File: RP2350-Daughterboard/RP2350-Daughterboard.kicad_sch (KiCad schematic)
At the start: 0 parts

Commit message: Added HDMI and PSRAM
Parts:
- added C1, C2: 15pF, symbol Device:C
- added C10, C3, C4, C7: 100nF, symbol Device:C
- added C5, C6: 4.7uF, symbol Device:C
- added C8: 1uF, Capacitor_SMD:C_0603_1608Metric, symbol Device:C
- added C9: 1uF, symbol Device:C
- added J1: ISA16_DAUGHTER_BUS, symbol W65C816-Computer:ISA16_DAUGHTER_BUS_98
- added J2: SWD, symbol Connector_Generic:Conn_01x05
- added J5: HDMI_A, symbol Connector:HDMI_A
- added L1: 2.2uH, symbol Device:L
- added R1: 1k, symbol Device:R
- added R10, R11, R12, R13, R6, R7, R8, R9: 270R, symbol Device:R
- added R14, R2, R3, R4, R5: 10k, symbol Device:R
- added SW1: BOOTSEL, symbol Switch:SW_Push
- added SW2: RESET, symbol Switch:SW_Push
- added U1: RP2354B, Package_DFN_QFN:QFN-80-1EP_10x10mm_P0.4mm_EP3.4x3.4mm, symbol MCU_RaspberryPi:RP2354B
- added U2: APS6404L-3SQR-SN, Package_SO:SOIC-8_3.9x4.9mm_P1.27mm, symbol Memory_RAM:APS6404L-3SQRx-SN
- added U3: TPD8F003, symbol Power_Protection:TPD8F003
- added Y1: 12MHz ABM8-272-T3, symbol Device:Crystal
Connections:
- new net +1V1: C4.1, C6.1, L1.2, U1.10 (DVDD), U1.32 (DVDD), U1.51 (DVDD), U1.65 (VREG_FB)
- new net +3V3: C10.1, C3.1, C5.1, C8.1, J1.2, J1.20, J1.42, J1.78, J2.1 (Pin_1), R14.1, R2.1, R3.1, R4.1, R5.1, U1.15 (IOVDD), U1.24 (IOVDD), U1.29 (IOVDD), U1.41 (IOVDD), U1.5 (IOVDD), U1.50 (IOVDD), U1.59 (ADC_AVDD), U1.60 (IOVDD), U1.61 (VREG_AVDD), U1.64 (VREG_VIN), U1.68 (USB_OTP_VDD), U1.69 (QSPI_IOVDD), U1.76 (IOVDD), U2.8 (VDD)
- new net +5V: C9.1, J1.38, J1.40, J5.18 (+5V)
- new net A0: J1.3, U1.77 (GPIO0)
- new net A1: J1.5, U1.78 (GPIO1)
- new net A10: J1.25
- new net A11: J1.27
- new net A12: J1.29
- new net A13: J1.31
- new net A14: J1.33
- new net A15: J1.35
- new net A16: J1.22
- new net A17: J1.24
- new net A18: J1.26
- new net A19: J1.28
- new net A2: J1.7, U1.79 (GPIO2)
- new net A20: J1.30
- new net A21: J1.32
- new net A22: J1.34
- new net A23: J1.36
- new net A3: J1.9, U1.80 (GPIO3)
- new net A4: J1.11, U1.1 (GPIO4)
- new net A5: J1.13, U1.2 (GPIO5)
- new net A6: J1.15, U1.3 (GPIO6)
- new net A7: J1.17, U1.4 (GPIO7)
- new net A8: J1.21, U1.6 (GPIO8)
- new net A9: J1.23, U1.7 (GPIO9)
- new net ABORT_N: J1.52
- new net AUDIO_IRQ: J1.71
- new net BANK00: J1.57
- new net BANK00_N: J1.58
- new net BE: J1.51
- new net DB_GPIO0: J1.74
- new net DB_GPIO1: J1.75
- new net DB_GPIO2: J1.76
- new net DB_GPIO3: J1.79
- new net DMA_ACK: J1.68
- new net DMA_REQ: J1.67
- new net E: J1.55
- new net EXP_CS_N: J1.73
- new net FRAME_IRQ: J1.70
- new net GND: C1.2, C10.2, C2.2, C3.2, C4.2, C5.2, C6.2, C7.2, C8.2, C9.2, J1.1, J1.19, J1.37, J1.39, J1.41, J1.77, J1.80, J2.2 (Pin_2), J5.11 (CKS), J5.17 (GND), J5.2 (D2S), J5.5 (D1S), J5.8 (D0S), J5.SH, SW1.2, SW2.2, U1.62 (VREG_PGND), U1.81 (GND), U2.4 (VSS), U3.17 (GND)
- new net HDMI_CK_N: J5.12 (CK-), R9.2, U3.13 (Ch4_Out), U3.4 (Ch4_In)
- new net HDMI_CK_P: J5.10 (CK+), R8.2, U3.14 (Ch3_Out), U3.3 (Ch3_In)
- new net HDMI_D0_N: J5.9 (D0-), R7.2, U3.15 (Ch2_Out), U3.2 (Ch2_In)
- new net HDMI_D0_P: J5.7 (D0+), R6.2, U3.1 (Ch1_In), U3.16 (Ch1_Out)
- new net HDMI_D1_N: J5.6 (D1-), R13.2, U3.8 (Ch8_In), U3.9 (Ch8_Out)
- new net HDMI_D1_P: J5.4 (D1+), R12.2, U3.10 (Ch7_Out), U3.7 (Ch7_In)
- new net HDMI_D2_N: J5.3 (D2-), R11.2, U3.11 (Ch6_Out), U3.6 (Ch6_In)
- new net HDMI_D2_P: J5.1 (D2+), R10.2, U3.12 (Ch5_Out), U3.5 (Ch5_In)
- new net HSTX_CK_N: R9.1, U1.14 (GPIO15)
- new net HSTX_CK_P: R8.1, U1.13 (GPIO14)
- new net HSTX_D0_N: R7.1, U1.12 (GPIO13)
- new net HSTX_D0_P: R6.1, U1.11 (GPIO12)
- new net HSTX_D1_N: R13.1, U1.19 (GPIO19)
- new net HSTX_D1_P: R12.1, U1.18 (GPIO18)
- new net HSTX_D2_N: R11.1, U1.17 (GPIO17)
- new net HSTX_D2_P: R10.1, U1.16 (GPIO16)
- new net IO_CS_N: J1.64
- new net IO_IRQ: J1.72
- new net IO_RD_N: J1.65
- new net IO_WR_N: J1.66
- new net IRQ_N: J1.47, U1.44 (GPIO35)
- new net MEM_OE_N: J1.59
- new net MEM_WE_N: J1.60
- new net MLB: J1.54
- new net MX: J1.56
- new net NMI_N: J1.48
- new net PHI2: J1.43, U1.36 (GPIO28)
- new net PSRAM_CS_N: R14.2, U1.58 (GPIO47/ADC7), U2.1 (~{CE})
- new net QSPI_CS_N: R3.2, SW1.1, U1.75 (~{QSPI_SS})
- new net QSPI_SCLK: U1.71 (QSPI_SCLK), U2.6 (SCLK)
- new net QSPI_SD0: U1.72 (QSPI_SD0), U2.5 (SI/SIO0)
- new net QSPI_SD1: U1.74 (QSPI_SD1), U2.2 (SO/SIO1)
- new net QSPI_SD2: R4.2, U1.73 (QSPI_SD2), U2.3 (SIO2)
- new net QSPI_SD3: R5.2, U1.70 (QSPI_SD3), U2.7 (SIO3)
- new net RAM_BLOCK0_N: J1.62
- new net RDY: J1.46, U1.43 (GPIO34)
- new net RESET_N: C7.1, J1.45, J2.5 (Pin_5), R2.2, SW2.1, U1.35 (RUN), U1.42 (GPIO33)
- new net ROM_CS_N: J1.61
- new net ROM_OVERLAY: J1.69
- new net RP_CS_N: J1.63, U1.40 (GPIO32)
- new net RP_D0: J1.4, U1.20 (GPIO20)
- new net RP_D1: J1.6, U1.21 (GPIO21)
- new net RP_D2: J1.8, U1.22 (GPIO22)
- new net RP_D3: J1.10, U1.23 (GPIO23)
- new net RP_D4: J1.12, U1.25 (GPIO24)
- new net RP_D5: J1.14, U1.26 (GPIO25)
- new net RP_D6: J1.16, U1.27 (GPIO26)
- new net RP_D7: J1.18, U1.28 (GPIO27)
- new net RWB: J1.44, U1.37 (GPIO29)
- new net SWCLK: J2.3 (Pin_3), U1.33 (SWCLK)
- new net SWDIO: J2.4 (Pin_4), U1.34 (SWDIO)
- new net VDA: J1.49, U1.38 (GPIO30)
- new net VPA: J1.50, U1.39 (GPIO31)
- new net VPB: J1.53
- new net VREG_LX: L1.1, U1.63 (VREG_LX)
- new net XIN: C1.1, U1.30 (XIN), Y1.1
- new net XOUT_CRYSTAL: C2.1, R1.2, Y1.2
- new net XOUT_DRIVE: R1.1, U1.31 (XOUT)
- no-connect marks 0 -> 23

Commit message: Added Readme introduction
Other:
- moved on the sheet: C1, C10, C2, C3, C4, C5, C6, C7, C8, C9, J1, J2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

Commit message: Fixed HDMI
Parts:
- removed U3: TPD8F003, symbol Power_Protection:TPD8F003
- added C11, C12, C13, C14, C15, C16, C17, C18, C19: 100nF, symbol Device:C
- added U3, U4: TPD4E05U06DQA, symbol Power_Protection:TPD4E05U06DQA
- C3, C4, C5, C6: footprint (none) -> Capacitor_SMD:C_0603_1608Metric
- R10, R11, R12, R13, R6, R7, R8, R9: footprint (none) -> Resistor_SMD:R_0603_1608Metric
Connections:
- net +1V1: now also C19.1
- net +3V3: now also C11.1, C12.1, C13.1, C14.1, C15.1, C16.1, C17.1, C18.1
- net GND: now also C11.2, C12.2, C13.2, C14.2, C15.2, C16.2, C17.2, C18.2, C19.2, U3.3 (GND), U3.8 (GND), U4.3 (GND), U4.8 (GND)
- net HDMI_CK_N: now also U3.5 (D2-)
- net HDMI_CK_P: now also U3.4 (D2+)
- net HDMI_D0_N: now also U3.2 (D1-)
- net HDMI_D0_P: now also U3.1 (D1+)
- net HDMI_D1_N: now also U4.5 (D2-)
- net HDMI_D1_P: now also U4.4 (D2+)
- net HDMI_D2_N: now also U4.2 (D1-)
- net HDMI_D2_P: now also U4.1 (D1+)
- no-connect marks 23 -> 31
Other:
- moved on the sheet: J5, R10, R11, R12, R13, R6, R7, R8, R9, SW1, SW2

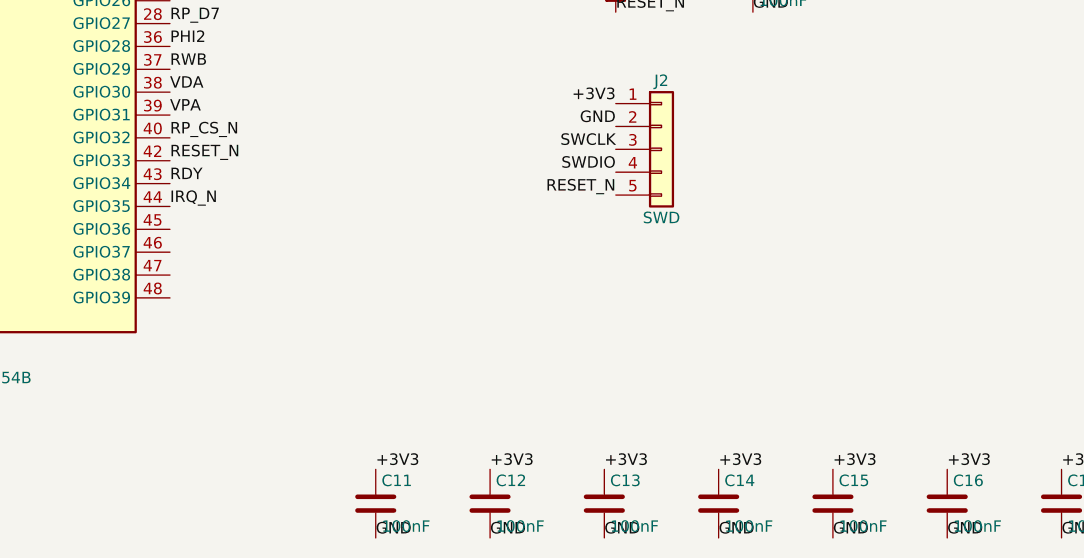
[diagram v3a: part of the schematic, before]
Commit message: Added buffer protection
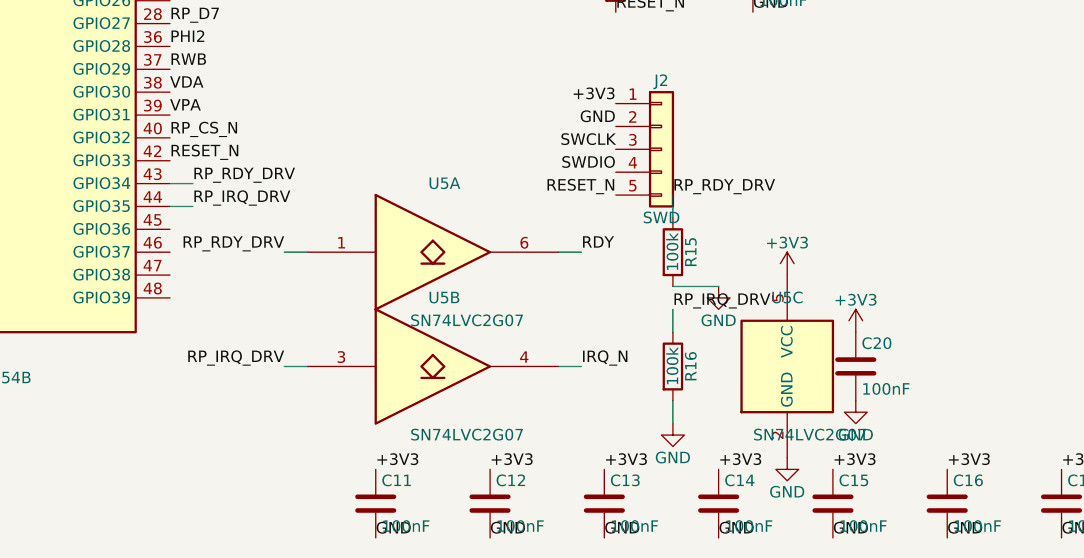
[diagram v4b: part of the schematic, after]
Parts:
- added C20: 100nF, symbol Device:C
- added R15, R16: 100k, symbol Device:R
- added U5: SN74LVC2G07, symbol 74xGxx:74LVC2G07
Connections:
- net +3V3: now also C20.1, U5.5 (VCC)
- net GND: now also C20.2, R15.2, R16.2, U5.2 (GND)
- net IRQ_N: now also U5.4; no longer U1.44 (GPIO35)
- net RDY: now also U5.6; no longer U1.43 (GPIO34)
- new net RP_IRQ_DRV: R16.1, U1.44 (GPIO35), U5.3
- new net RP_RDY_DRV: R15.1, U1.43 (GPIO34), U5.1

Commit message: Added VBus, SD card, ESP-C3 and W5500
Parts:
- added C21, C23, C25: 10uF, Capacitor_SMD:C_0805_2012Metric, symbol Device:C
- added C22, C24, C26: 100nF, Capacitor_SMD:C_0805_2012Metric, symbol Device:C
- added C27, C28, C29, C30: 100nF, Capacitor_SMD:C_0603_1608Metric, symbol Device:C
- added J3: USB-A PORT 1, symbol Connector:USB_A
- added J4: USB-A PORT 2, symbol Connector:USB_A
- added J6: USB 2.0 FRONT PANEL (KEYED), symbol Connector_Generic:Conn_02x05_Odd_Even
- added J7: SD_Card_Receptacle, Connector_Card:SD_Kyocera_145638109211859+, symbol Connector:SD_Card_Receptacle
- added J8: Conn_Coaxial, Connector_Coaxial:SMA_BAT_Wireless_BWSMA-KWE-Z001, symbol Connector:Conn_Coaxial
- added J9: RJ45, Connector_RJ:RJ45_Amphenol_54602-x08_Horizontal, symbol Connector:RJ45
- added R17: 2.7k 1%, Resistor_SMD:R_0805_2012Metric, symbol Device:R
- added R18: 10k, Resistor_SMD:R_0805_2012Metric, symbol Device:R
- added U10, U7, U8, U9: TPS2051CDBV, Package_TO_SOT_SMD:SOT-23-5, symbol Power_Management:TPS2051CDBV
- added U11: ESP32-C3, Package_DFN_QFN:QFN-32-1EP_5x5mm_P0.5mm_EP3.7x3.7mm, symbol MCU_Espressif:ESP32-C3
- added U12: W5500, Package_QFP:LQFP-48_7x7mm_P0.5mm, symbol Interface_Ethernet:W5500
- added U6: FE1.1s, Package_SO:SSOP-28_3.9x9.9mm_P0.635mm, symbol Interface_USB:FE1.1s
- added Y2: 12MHz, Crystal:Crystal_SMD_5032-2Pin_5.0x3.2mm, symbol Device:Crystal
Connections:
- net +3V3: now also R18.1, U10.4 (EN), U6.19 (BUSJ), U7.4 (EN), U8.4 (EN), U9.4 (EN)
- net +5V: now also C25.1, C26.1, C27.1, C28.1, C29.1, C30.1, U10.5 (IN), U6.18 (VBUSM), U6.20 (VDD5), U7.5 (IN), U8.5 (IN), U9.5 (IN)
- net GND: now also C21.2, C22.2, C23.2, C24.2, C25.2, C26.2, C27.2, C28.2, C29.2, C30.2, J3.4 (GND), J3.SH (Shield), J4.4 (GND), J4.SH (Shield), J6.7 (Pin_7), J6.8 (Pin_8), R17.2, U10.2 (GND), U6.1 (VSS), U7.2 (GND), U8.2 (GND), U9.2 (GND)
- net RESET_N: now also U6.17 (~{XRSTJ})
- net USB_DM: now reaches U1.66 (USB_DM)
- net USB_DM: now also U6.15 (DMU)
- net USB_DP: now reaches U1.67 (USB_DP)
- net USB_DP: now also U6.16 (DPU)
- new net: C21.1, C22.1, U6.13 (VD33), U6.21 (VD33_O)
- new net: U12.11 (AVDD), U12.15 (AVDD), U12.17 (AVDD), U12.21 (AVDD), U12.4 (AVDD), U12.8 (AVDD)
- new net: U12.14 (AGND), U12.16 (AGND), U12.19 (AGND), U12.3 (AGND), U12.48 (AGND), U12.9 (AGND)
- new net: U11.2 (VDD3P3), U11.3 (VDD3P3)
- new net: U11.31 (VDDA), U11.32 (VDDA)
- new net: J7.3 (VSS), J7.6 (VSS)
- new net USB1_DM: J3.2 (D-), U6.10 (DM1)
- new net USB1_DP: J3.3 (D+), U6.11 (DP1)
- new net USB1_OC_N: U7.3 (~{FLT})
- new net USB1_VBUS: J3.1 (VBUS), U7.1 (OUT)
- new net USB2_DM: J4.2 (D-), U6.8 (DM2)
- new net USB2_DP: J4.3 (D+), U6.9 (DP2)
- new net USB2_OC_N: U8.3 (~{FLT})
- new net USB2_VBUS: J4.1 (VBUS), U8.1 (OUT)
- new net USB3_DM: J6.3 (Pin_3), U6.6 (DM3)
- new net USB3_DP: J6.5 (Pin_5), U6.7 (DP3)
- new net USB3_OC_N: U9.3 (~{FLT})
- new net USB3_VBUS: J6.1 (Pin_1), U9.1 (OUT)
- new net USB4_DM: J6.4 (Pin_4), U6.4 (DM4)
- new net USB4_DP: J6.6 (Pin_6), U6.5 (DP4)
- new net USB4_OC_N: U10.3 (~{FLT})
- new net USB4_VBUS: J6.2 (Pin_2), U10.1 (OUT)
- new net USB_HUB_1V8: C23.1, C24.1, U6.12 (VD18_O), U6.28 (VD18)
- new net USB_HUB_PWR_EN_N: U6.25 (PWRJ)
- new net USB_HUB_REXT: R17.1, U6.14 (REXT)
- new net USB_HUB_XIN: U6.3 (XIN), Y2.2
- new net USB_HUB_XOUT: U6.2 (XOUT), Y2.1
- new net USB_OC_N: R18.2, U6.26 (OVCJ)
- no-connect marks 31 -> 37

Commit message: replaced esp
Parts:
- removed J8: Conn_Coaxial, Connector_Coaxial:SMA_BAT_Wireless_BWSMA-KWE-Z001, symbol Connector:Conn_Coaxial
- removed U11: ESP32-C3, Package_DFN_QFN:QFN-32-1EP_5x5mm_P0.5mm_EP3.7x3.7mm, symbol MCU_Espressif:ESP32-C3
- added U11: ESP32-C3-WROOM-02U, RF_Module:ESP32-C3-WROOM-02U, symbol RF_Module:ESP32-C3-WROOM-02U
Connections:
- net +3V3: now also J7.4 (VDD)
- net GND: now also J7.3 (VSS), J7.6 (VSS), J7.SH (SHELL)
- net SD_CLK: now reaches U1.49 (GPIO40/ADC0)
- net SD_CLK: now also J7.5 (CLK)
- net SD_CMD: now reaches U1.52 (GPIO41/ADC1)
- net SD_CMD: now also J7.2 (CMD)
- net SD_DAT0: now reaches U1.53 (GPIO42/ADC2)
- net SD_DAT0: now also J7.7 (DAT0)
- net SD_CS_N: now reaches U1.54 (GPIO43/ADC3)
- net SD_CS_N: now also J7.1 (CD/DAT3)
- new net: U11.19 (GND), U11.9 (GND)
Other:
- moved on the sheet: J9

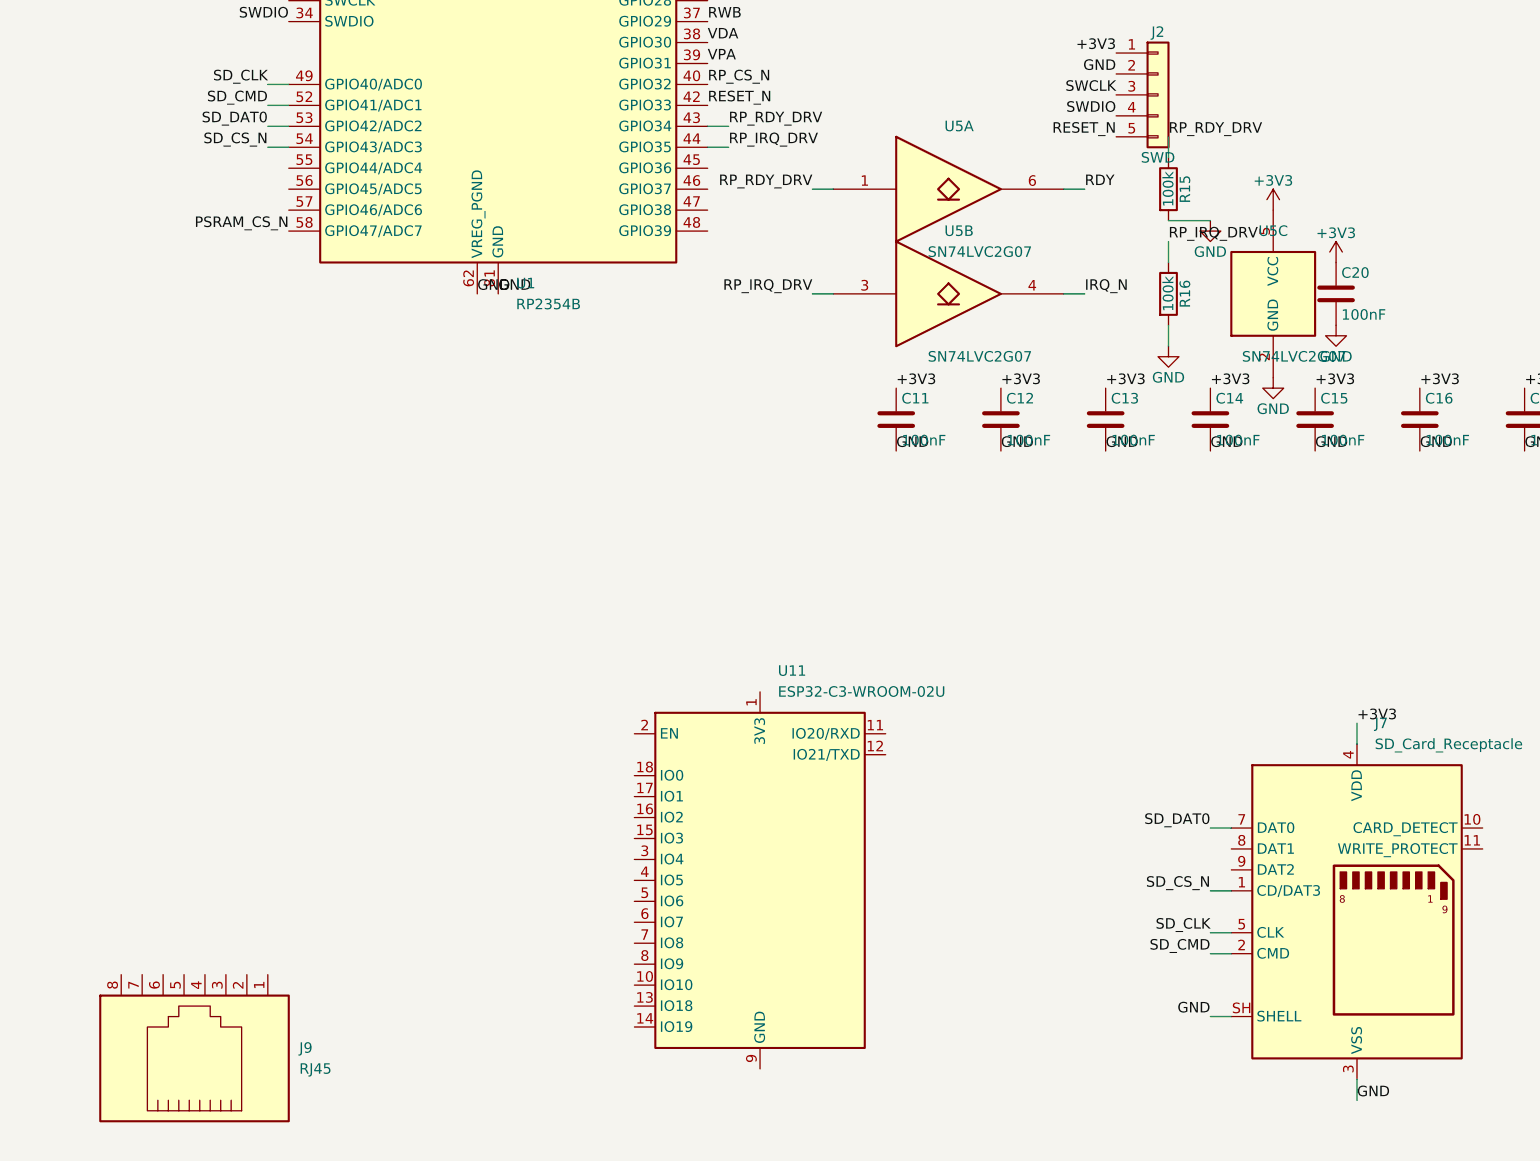
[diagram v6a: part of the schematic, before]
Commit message: wired ESP to RP
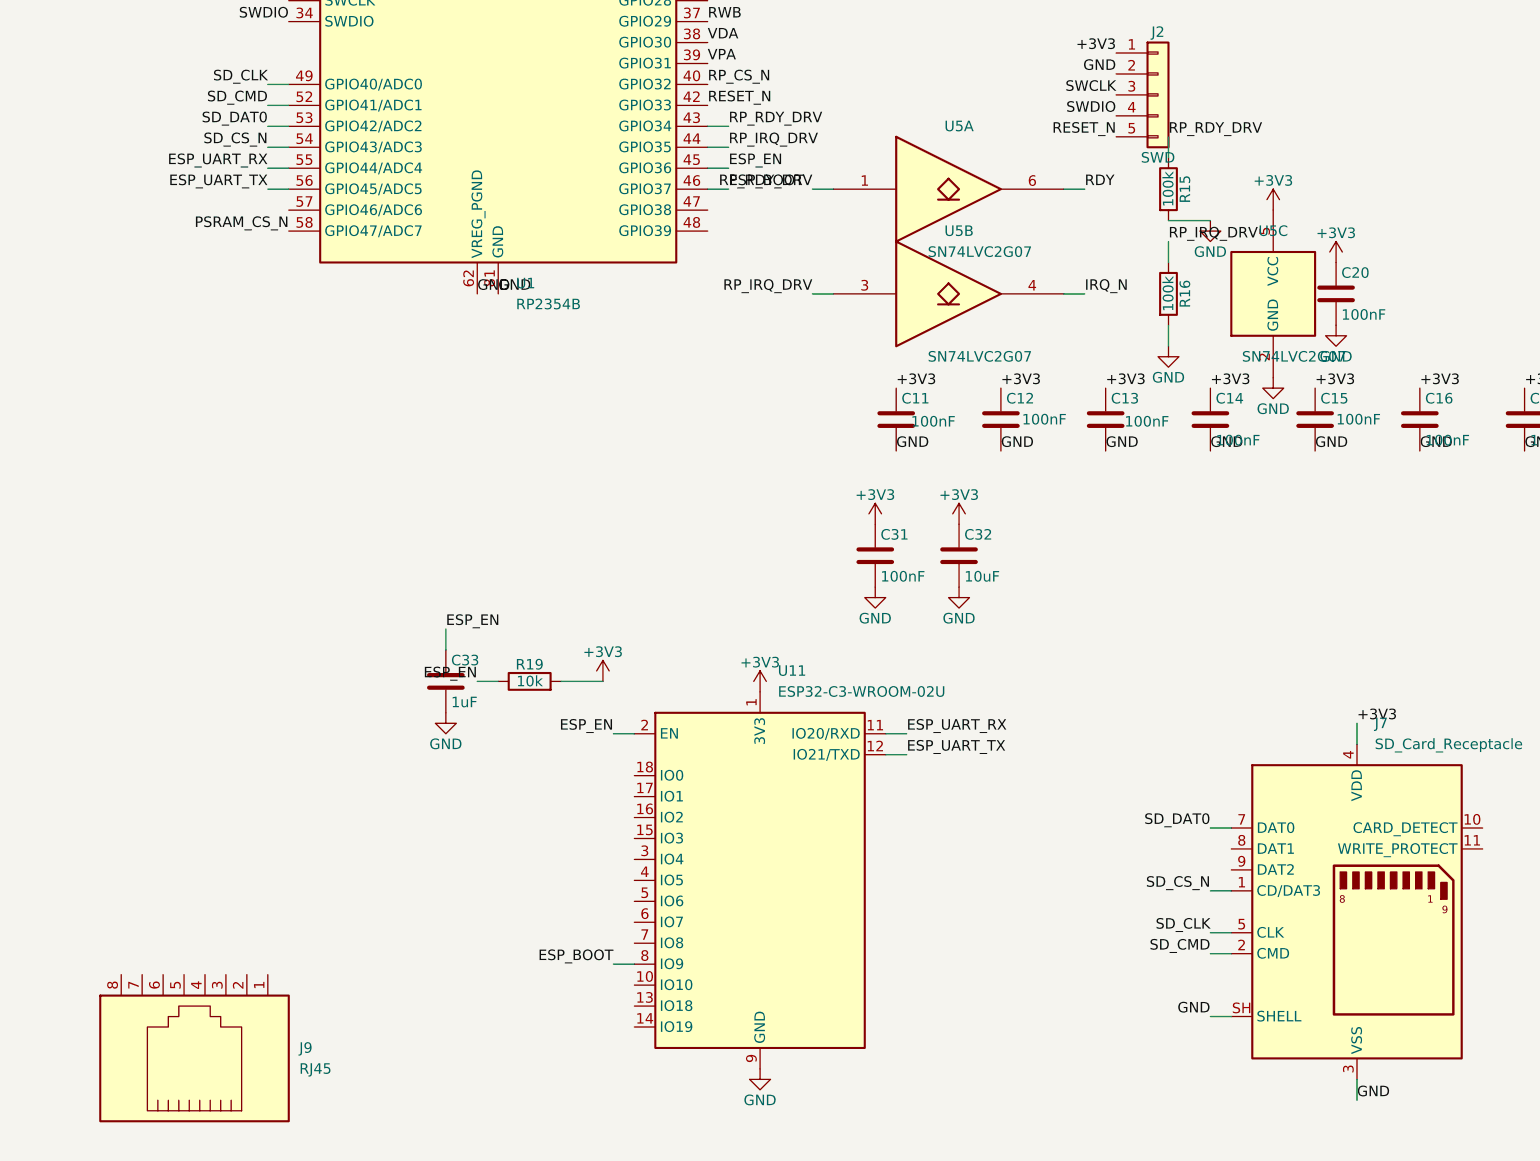
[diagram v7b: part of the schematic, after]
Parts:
- added C31: 100nF, Capacitor_SMD:C_0603_1608Metric, symbol Device:C
- added C32: 10uF, Capacitor_SMD:C_0805_2012Metric, symbol Device:C
- added C33: 1uF, Capacitor_SMD:C_0603_1608Metric, symbol Device:C
- added R19: 10k, Resistor_SMD:R_0603_1608Metric, symbol Device:R
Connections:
- net +3V3: now also U11.1 (3V3), C31.1, C32.1, R19.2
- net GND: now also U11.19 (GND), U11.9 (GND), C31.2, C32.2, C33.2
- net ESP_EN: now reaches U1.45 (GPIO36)
- net ESP_EN: now also U11.2 (EN), C33.1, R19.1
- net ESP_BOOT: now reaches U1.46 (GPIO37)
- net ESP_BOOT: now also U11.8 (IO9)
- net ESP_UART_RX: now reaches U1.55 (GPIO44/ADC4)
- net ESP_UART_RX: now also U11.11 (IO20/RXD)
- net ESP_UART_TX: now reaches U1.56 (GPIO45/ADC5)
- net ESP_UART_TX: now also U11.12 (IO21/TXD)
